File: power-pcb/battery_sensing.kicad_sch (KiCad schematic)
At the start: 14 parts, among them J6 JST PH, J7 JST PH, U7 RFM-0505S, U8 DS2484R, U9 RFM-0505S

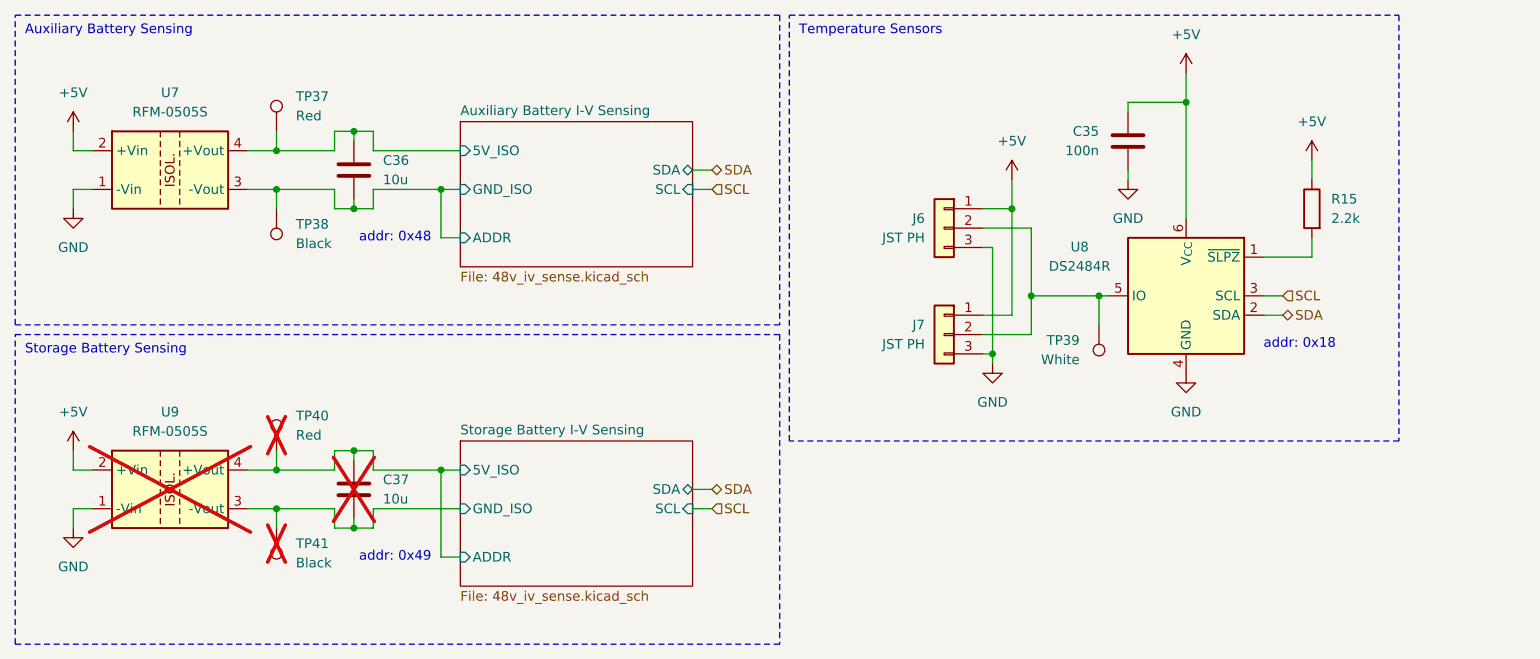
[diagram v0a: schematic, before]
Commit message: power-pcb: re-annotate schematic and start board
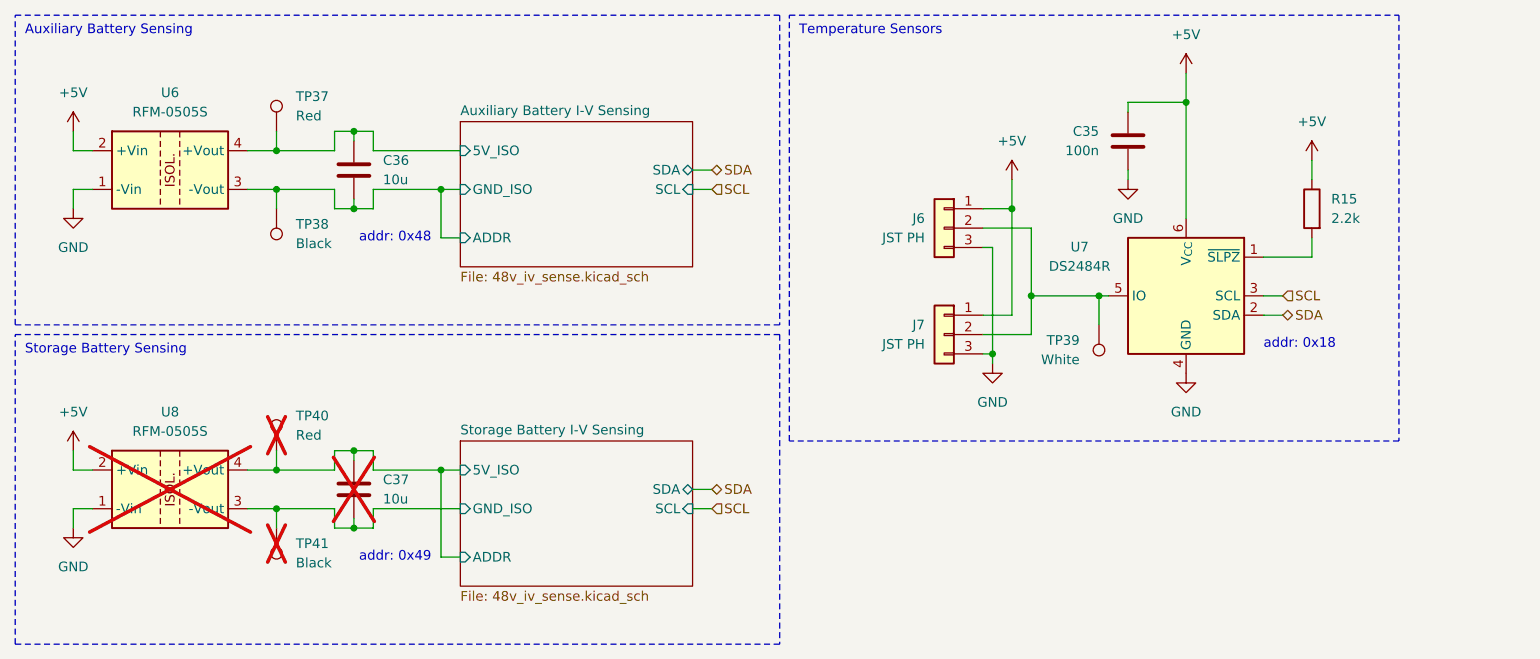
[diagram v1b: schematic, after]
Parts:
- renumbered U7 to U6, U8 to U7, U9 to U8
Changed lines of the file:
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@@
 		(dnp yes)
 		(fields_autoplaced yes)
-		(property "Reference" "U9"
+		(property "Reference" "U8"
 			(at 33.02 64.77 0)
 			(show_name no)
@@
 			(project "power-pcb"
 				(path "/4b4cf3aa-c94c-4150-b9c5-35049cd71136/50636587-2815-4d8e-b0bd-5f3d88757853"
-					(reference "U9")
+					(reference "U8")
 					(unit 1)
 					(variant
@@
 		(dnp no)
 		(fields_autoplaced yes)
-		(property "Reference" "U7"
+		(property "Reference" "U6"
 			(at 33.02 22.86 0)
 			(show_name no)
@@
 			(project "power-pcb"
 				(path "/4b4cf3aa-c94c-4150-b9c5-35049cd71136/50636587-2815-4d8e-b0bd-5f3d88757853"
-					(reference "U7")
+					(reference "U6")
 					(unit 1)
 					(variant
@@
 		(dnp no)
 		(fields_autoplaced yes)
-		(property "Reference" "U8"
+		(property "Reference" "U7"
 			(at 152.4 43.1098 0)
 			(show_name no)
@@
 			(project "power-pcb"
 				(path "/4b4cf3aa-c94c-4150-b9c5-35049cd71136/50636587-2815-4d8e-b0bd-5f3d88757853"
-					(reference "U8")
+					(reference "U7")
 					(unit 1)
 					(variant

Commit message: power-pcb: fix schematic after review
- Add footprint for resitive load for the RECOM
- Add Opamps when useful
- Add capacitor and change some footprint sizes
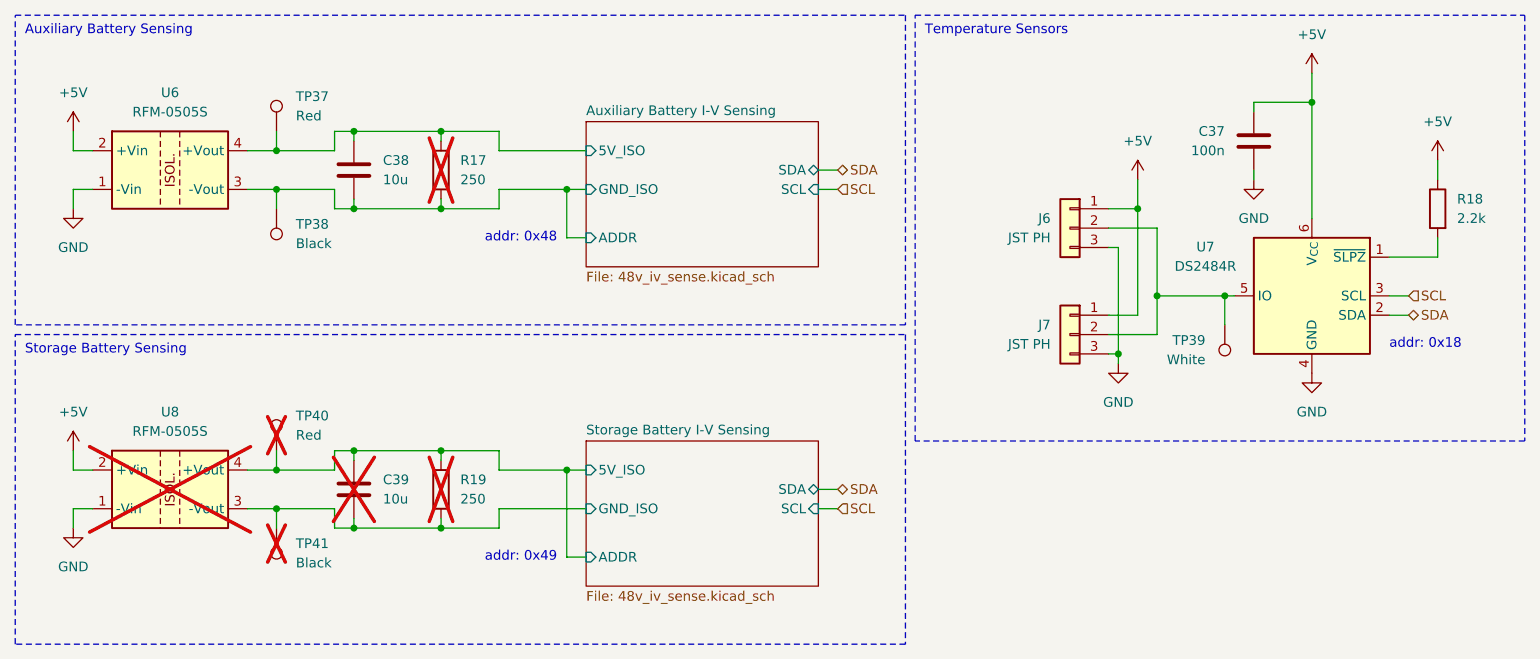
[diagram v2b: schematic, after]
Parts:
- added R17, R19: 250, Resistor_THT:R_Axial_DIN0309_L9.0mm_D3.2mm_P12.70mm_Horizontal, symbol Device:R
- C37: renamed from C35; footprint Capacitor_SMD:C_0603_1608Metric_Pad1.08x0.95mm_HandSolder -> Capacitor_SMD:C_0402_1005Metric_Pad0.74x0.62mm_HandSolder; JLCPCB C14663 -> C307331
- renumbered C36 to C38, C37 to C39, R15 to R18
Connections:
- net Auxiliary Battery I-V Sensing/5V_ISO: now also R17.1
- net Auxiliary Battery I-V Sensing/ADDR: now also R17.2
- net Storage Battery I-V Sensing/5V_ISO: now also R19.1
- net Storage Battery I-V Sensing/GND_ISO: now also R19.2
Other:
- moved on the sheet: C37, J6, J7, R18, TP39, U7
